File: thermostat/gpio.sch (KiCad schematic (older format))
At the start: 19 parts, among them J5 Conn_01x20, Q4 BC817, Q5 BC817, Q6 BC817, U8 PCF8574

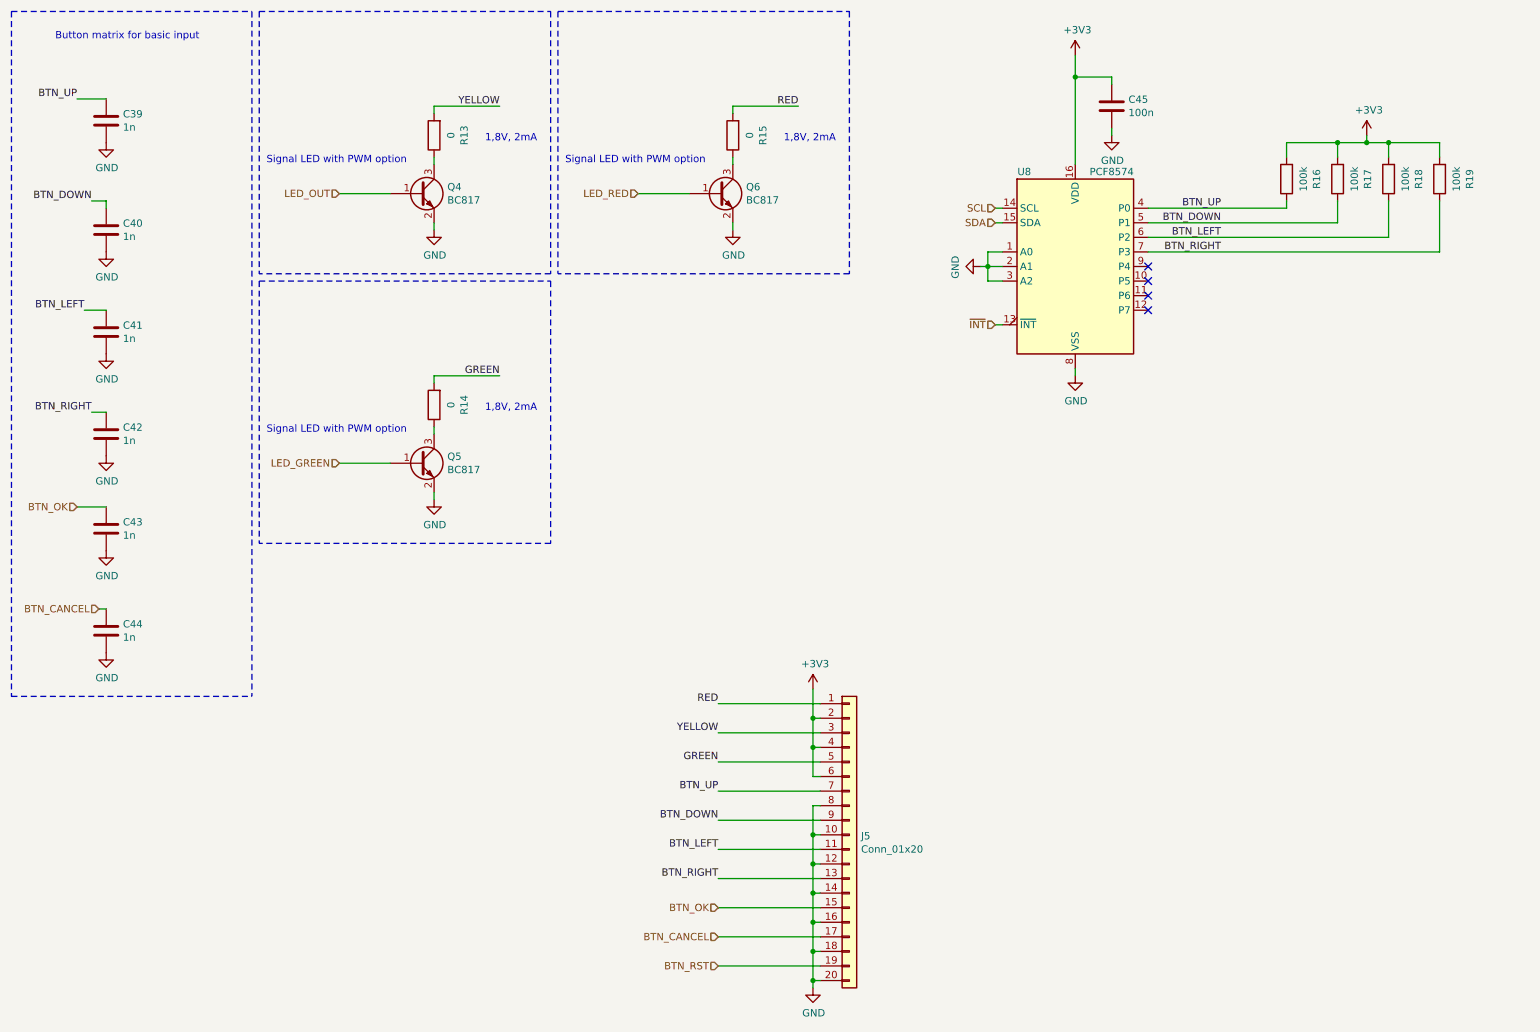
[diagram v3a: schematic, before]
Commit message: Fine grouping of parts done, may start routing . GPIO connector on wrong side of PCB (I wanted to have the buttons on the opposite side, but thats not a big problem.
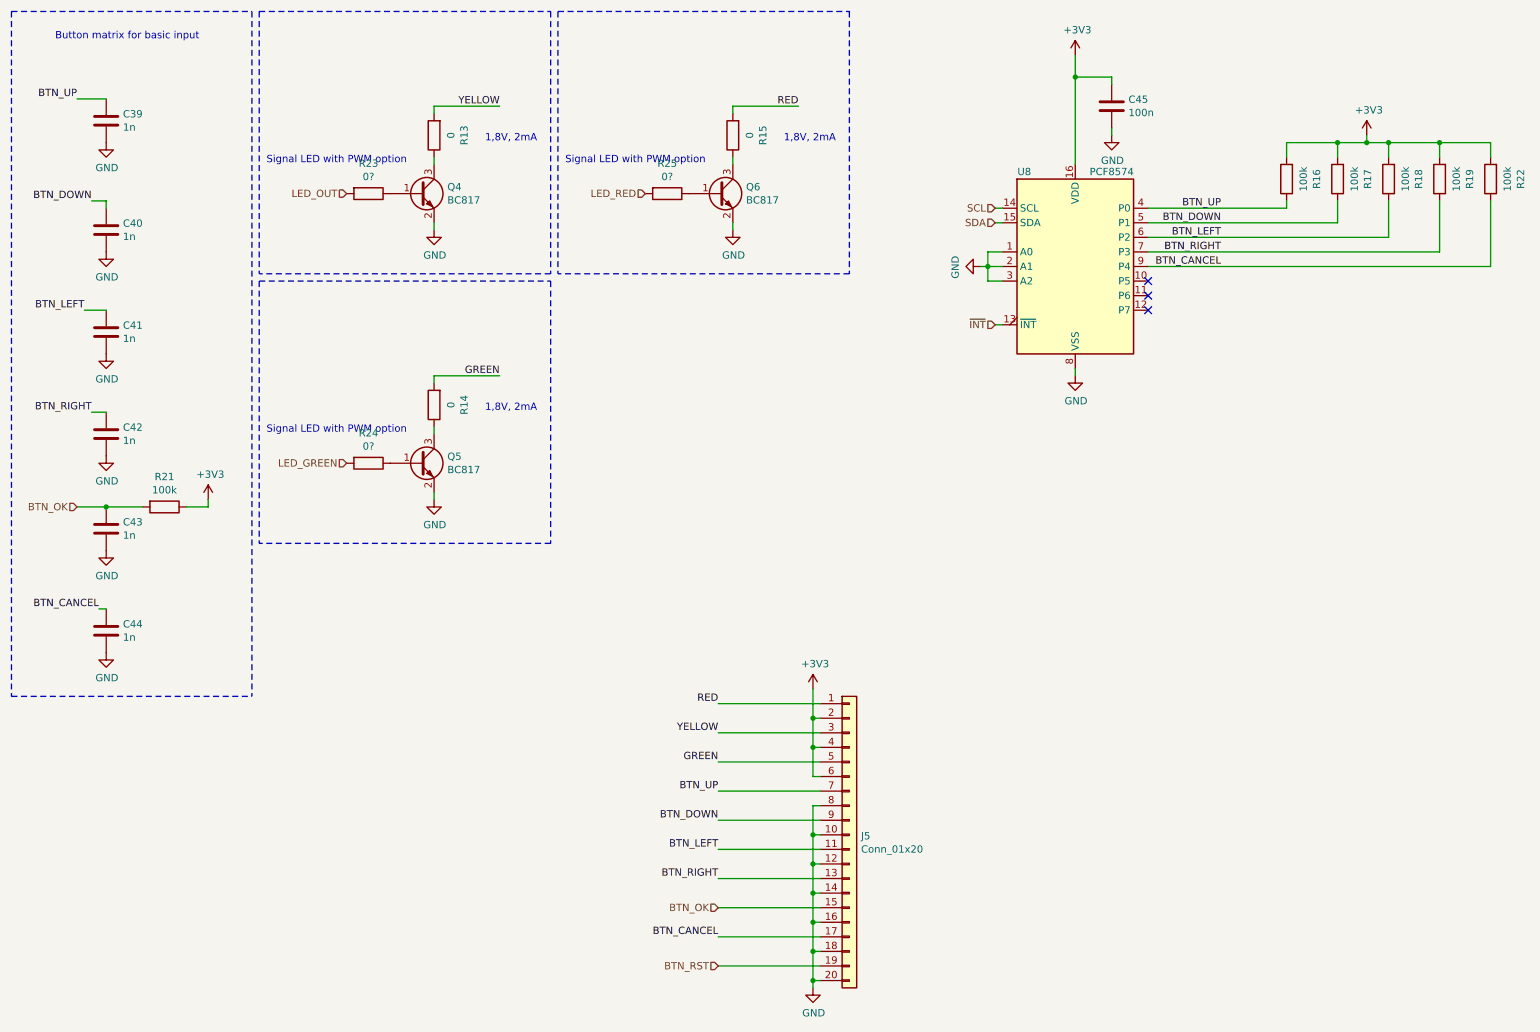
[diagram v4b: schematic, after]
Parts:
- added R21, R22: 100k, Resistor_SMD:R_0402_1005Metric, symbol Device:R
- added R23, R24, R25: 0?, Resistor_SMD:R_0402_1005Metric, symbol Device:R
- C39, C40, C41, C42, C43, C44: footprint Capacitor_SMD:C_0603_1608Metric -> Capacitor_SMD:C_0402_1005Metric
- R16, R17, R18, R19: footprint Resistor_SMD:R_0603_1608Metric -> Resistor_SMD:R_0402_1005Metric
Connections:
- net +3V3: now also R21.1, R22.2
- net BTN_CANCEL: now also U8.9 (P4), R22.1
- net BTN_OK: now also R21.2
- net LED_GREEN: now also R24.2; no longer Q5.1 (B)
- net LED_OUT: now also R23.2; no longer Q4.1 (B)
- net LED_RED: now also R25.2; no longer Q6.1 (B)
- new net: Q6.1 (B), R25.1
- new net: Q4.1 (B), R23.1
- new net: Q5.1 (B), R24.1
- no-connect marks 4 -> 3
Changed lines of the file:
@@
 Wire Wire Line
 	5600 1600 5600 1650
-Wire Wire Line
-	4950 1850 5300 1850
 $Comp
 L Device:R R?
@@
 Wire Wire Line
 	3550 1600 3550 1650
-Wire Wire Line
-	2900 1850 3250 1850
 $Comp
 L Device:R R?
@@
 Wire Wire Line
 	3550 3450 3550 3500
-Wire Wire Line
-	2900 3700 3250 3700
 $Comp
 L Device:C C44
@@
 F 0 "C44" H 1415 4896 50  0000 L CNN
 F 1 "1n" H 1415 4805 50  0000 L CNN
-F 2 "Capacitor_SMD:C_0603_1608Metric" H 1338 4700 50  0001 C CNN
+F 2 "Capacitor_SMD:C_0402_1005Metric" H 1338 4700 50  0001 C CNN
 F 3 "~" H 1300 4850 50  0001 C CNN
 	1    1300 4850
@@
 F 0 "C43" H 1415 4196 50  0000 L CNN
 F 1 "1n" H 1415 4105 50  0000 L CNN
-F 2 "Capacitor_SMD:C_0603_1608Metric" H 1338 4000 50  0001 C CNN
+F 2 "Capacitor_SMD:C_0402_1005Metric" H 1338 4000 50  0001 C CNN
 F 3 "~" H 1300 4150 50  0001 C CNN
 	1    1300 4150
@@
 F 0 "C42" H 1415 3546 50  0000 L CNN
 F 1 "1n" H 1415 3455 50  0000 L CNN
-F 2 "Capacitor_SMD:C_0603_1608Metric" H 1338 3350 50  0001 C CNN
+F 2 "Capacitor_SMD:C_0402_1005Metric" H 1338 3350 50  0001 C CNN
 F 3 "~" H 1300 3500 50  0001 C CNN
 	1    1300 3500
@@
 F 0 "C41" H 1415 2846 50  0000 L CNN
 F 1 "1n" H 1415 2755 50  0000 L CNN
-F 2 "Capacitor_SMD:C_0603_1608Metric" H 1338 2650 50  0001 C CNN
+F 2 "Capacitor_SMD:C_0402_1005Metric" H 1338 2650 50  0001 C CNN
 F 3 "~" H 1300 2800 50  0001 C CNN
 	1    1300 2800
@@
 F 0 "C40" H 1415 2146 50  0000 L CNN
 F 1 "1n" H 1415 2055 50  0000 L CNN
-F 2 "Capacitor_SMD:C_0603_1608Metric" H 1338 1950 50  0001 C CNN
+F 2 "Capacitor_SMD:C_0402_1005Metric" H 1338 1950 50  0001 C CNN
 F 3 "~" H 1300 2100 50  0001 C CNN
 	1    1300 2100
@@
 F 0 "C39" H 1415 1396 50  0000 L CNN
 F 1 "1n" H 1415 1305 50  0000 L CNN
-F 2 "Capacitor_SMD:C_0603_1608Metric" H 1338 1200 50  0001 C CNN
+F 2 "Capacitor_SMD:C_0402_1005Metric" H 1338 1200 50  0001 C CNN
 F 3 "~" H 1300 1350 50  0001 C CNN
 	1    1300 1350
@@
 Wire Notes Line
 	2350 600  2350 2400
-Text HLabel 1100 4000 0    50   Input ~ 0
-BTN_OK
-Text HLabel 1250 4700 0    50   Input ~ 0
-BTN_CANCEL
-Text HLabel 2900 1850 0    50   Input ~ 0
+Text HLabel 2950 1850 0    50   Input ~ 0
 LED_OUT
-Text HLabel 4950 1850 0    50   Input ~ 0
+Text HLabel 5000 1850 0    50   Input ~ 0
 LED_RED
-Text HLabel 2900 3700 0    50   Input ~ 0
+Text HLabel 2950 3700 0    50   Input ~ 0
 LED_GREEN
 Text Label 1100 1200 2    50   ~ 0
@@
 F 0 "R16" V 9193 1750 50  0000 C CNN
 F 1 "100k" V 9284 1750 50  0000 C CNN
-F 2 "Resistor_SMD:R_0603_1608Metric" V 9330 1750 50  0001 C CNN
+F 2 "Resistor_SMD:R_0402_1005Metric" V 9330 1750 50  0001 C CNN
 F 3 "~" H 9400 1750 50  0001 C CNN
 	1    9400 1750
@@
 F 0 "R17" V 9543 1750 50  0000 C CNN
 F 1 "100k" V 9634 1750 50  0000 C CNN
-F 2 "Resistor_SMD:R_0603_1608Metric" V 9680 1750 50  0001 C CNN
+F 2 "Resistor_SMD:R_0402_1005Metric" V 9680 1750 50  0001 C CNN
 F 3 "~" H 9750 1750 50  0001 C CNN
 	1    9750 1750
@@
 F 0 "R18" V 9893 1750 50  0000 C CNN
 F 1 "100k" V 9984 1750 50  0000 C CNN
-F 2 "Resistor_SMD:R_0603_1608Metric" V 10030 1750 50  0001 C CNN
+F 2 "Resistor_SMD:R_0402_1005Metric" V 10030 1750 50  0001 C CNN
 F 3 "~" H 10100 1750 50  0001 C CNN
 	1    10100 1750
@@
 F 0 "R19" V 10243 1750 50  0000 C CNN
 F 1 "100k" V 10334 1750 50  0000 C CNN
-F 2 "Resistor_SMD:R_0603_1608Metric" V 10380 1750 50  0001 C CNN
+F 2 "Resistor_SMD:R_0402_1005Metric" V 10380 1750 50  0001 C CNN
 F 3 "~" H 10450 1750 50  0001 C CNN
 	1    10450 1750
@@
 Wire Wire Line
 	7950 1050 7950 1650
-NoConn ~ 8450 2350
 NoConn ~ 8450 2450
 NoConn ~ 8450 2550
@@
 Wire Wire Line
 	5500 7150 6200 7150
-Text HLabel 5500 6950 0    50   Input ~ 0
-BTN_CANCEL
-Text HLabel 5500 6750 0    50   Input ~ 0
-BTN_OK
 Text Label 5500 6550 2    50   ~ 0
 BTN_RIGHT
@@
 Text Label 4000 3100 2    50   ~ 0
 GREEN
+$Comp
+L power:+3V3 #PWR?
+U 1 1 5FA8BBB8
+P 2000 3950
+AR Path="/5E8AC4D3/5FA8BBB8" Ref="#PWR?"  Part="1"
+AR Path="/5FA8BBB8" Ref="#PWR?"  Part="1"
+AR Path="/5F39C8C1/5FA8BBB8" Ref="#PWR0115"  Part="1"
+F 0 "#PWR0115" H 2000 3800 50  0001 C CNN
+F 1 "+3V3" H 2015 4123 50  0000 C CNN
+F 2 "" H 2000 3950 50  0001 C CNN
+F 3 "" H 2000 3950 50  0001 C CNN
+	1    2000 3950
+	1    0    0    -1
+$EndComp
+$Comp
+L Device:R R?
+U 1 1 5FA8C1EC
+P 1700 4000
+AR Path="/5E6A63AE/5FA8C1EC" Ref="R?"  Part="1"
+AR Path="/5FA8C1EC" Ref="R?"  Part="1"
+AR Path="/5F39C8C1/5FA8C1EC" Ref="R21"  Part="1"
+F 0 "R21" V 1493 4000 50  0000 C CNN
+F 1 "100k" V 1584 4000 50  0000 C CNN
+F 2 "Resistor_SMD:R_0402_1005Metric" V 1630 4000 50  0001 C CNN
+F 3 "~" H 1700 4000 50  0001 C CNN
+	1    1700 4000
+	0    1    1    0
+$EndComp
+Wire Wire Line
+	1300 4000 1550 4000
+Connection ~ 1300 4000
+Wire Wire Line
+	1850 4000 2000 4000
+Wire Wire Line
+	2000 4000 2000 3950
+Text HLabel 1100 4000 0    50   Input ~ 0
+BTN_OK
+Text HLabel 5500 6750 0    50   Input ~ 0
+BTN_OK
+Text Label 5500 6950 2    50   ~ 0
+BTN_CANCEL
+Text Label 1250 4700 2    50   ~ 0
+BTN_CANCEL
+$Comp
+L Device:R R?
+U 1 1 5FA930FA
+P 10800 1750
+AR Path="/5E6A63AE/5FA930FA" Ref="R?"  Part="1"
+AR Path="/5FA930FA" Ref="R?"  Part="1"
+AR Path="/5F39C8C1/5FA930FA" Ref="R22"  Part="1"
+F 0 "R22" V 10593 1750 50  0000 C CNN
+F 1 "100k" V 10684 1750 50  0000 C CNN
+F 2 "Resistor_SMD:R_0402_1005Metric" V 10730 1750 50  0001 C CNN
+F 3 "~" H 10800 1750 50  0001 C CNN
+	1    10800 1750
+	-1   0    0    1
+$EndComp
+Wire Wire Line
+	10800 1600 10800 1500
+Wire Wire Line
+	10800 1500 10450 1500
+Connection ~ 10450 1500
+Wire Wire Line
+	8450 2350 10800 2350
+Wire Wire Line
+	10800 2350 10800 1900
+Text Label 8950 2350 2    50   ~ 0
+BTN_CANCEL
+$Comp
+L Device:R R?
+U 1 1 5FAA9C4A
+P 3100 1850
+AR Path="/5E6A63AE/5FAA9C4A" Ref="R?"  Part="1"
+AR Path="/5FAA9C4A" Ref="R?"  Part="1"
+AR Path="/5F39C8C1/5FAA9C4A" Ref="R23"  Part="1"
+F 0 "R23" V 2893 1850 50  0000 C CNN
+F 1 "0?" V 2984 1850 50  0000 C CNN
+F 2 "Resistor_SMD:R_0402_1005Metric" V 3030 1850 50  0001 C CNN
+F 3 "~" H 3100 1850 50  0001 C CNN
+	1    3100 1850
+	0    1    1    0
+$EndComp
+$Comp
+L Device:R R?
+U 1 1 5FAAA4F5
+P 5150 1850
+AR Path="/5E6A63AE/5FAAA4F5" Ref="R?"  Part="1"
+AR Path="/5FAAA4F5" Ref="R?"  Part="1"
+AR Path="/5F39C8C1/5FAAA4F5" Ref="R25"  Part="1"
+F 0 "R25" V 4943 1850 50  0000 C CNN
+F 1 "0?" V 5034 1850 50  0000 C CNN
+F 2 "Resistor_SMD:R_0402_1005Metric" V 5080 1850 50  0001 C CNN
+F 3 "~" H 5150 1850 50  0001 C CNN
+	1    5150 1850
+	0    1    1    0
+$EndComp
+$Comp
+L Device:R R?
+U 1 1 5FAAA7FD
+P 3100 3700
+AR Path="/5E6A63AE/5FAAA7FD" Ref="R?"  Part="1"
+AR Path="/5FAAA7FD" Ref="R?"  Part="1"
+AR Path="/5F39C8C1/5FAAA7FD" Ref="R24"  Part="1"
+F 0 "R24" V 2893 3700 50  0000 C CNN
+F 1 "0?" V 2984 3700 50  0000 C CNN
+F 2 "Resistor_SMD:R_0402_1005Metric" V 3030 3700 50  0001 C CNN
+F 3 "~" H 3100 3700 50  0001 C CNN
+	1    3100 3700
+	0    1    1    0
+$EndComp
 $EndSCHEMATC
